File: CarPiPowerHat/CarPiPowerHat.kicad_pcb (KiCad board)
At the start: 4 copper layers, 96 x 85 mm, 118 parts, among them J1 HDMI_A_1.4, J2 1-84953-5, J3 40HAT, J4 Conn_02x03_Counter_Clockwise, J5 USB_A, J6 1-84953-5, J7 HDMI_A_1.4, J8 AudioJack2_Ground, Q1 DMG2305, Q1 DMMT5401, Q2 DMG2305UX, Q3 DMP3013SFV-7, U1 AP64501SP-13, U1 UDA1334ATS, U2 AP2112-3.3K, U2 CAT24C32, U3 LM3480-5.0, U4 ATtiny45V-10X, U5 PCF85063AT/AAZ, U6 RT9742SNGV, U8 UDA1334ATS, X2 19269, Y1 X32K768S301

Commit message: doing some traces
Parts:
- removed the C1 at (51.8, 100.4)
- removed the C11 at (29.0, 86.7)
- removed the C13 at (29.9, 92.9)
- removed the C14 at (51.3, 89.6)
- removed the C2 at (51.3, 91.4)
- removed the C3 at (55.7, 87.1)
- removed the C4 at (45.9, 99.5)
- removed the C5 at (50.3, 100.4)
- removed the C6 at (46.6, 90.5)
- removed the C7 at (39.7, 88.7)
- removed the C8 at (42.2, 99.5)
- removed the FB2 at (34.3, 88.2)
- removed the Q1 at (55.7, 90.7)
- removed the R1 at (56.9, 93.4)
- removed the R2 at (55.7, 88.3)
- removed the R3 at (42.2, 87.8)
- removed the R4 at (42.1, 89.6)
- removed the R5 at (48.7, 104.1)
- removed the R6 at (45.5, 104.1)
- removed the U1 at (52.2, 95.3)
- removed the U2 at (29.7, 89.7)
- removed X2: 19269, Adafruit I2S Audio UDA1334 Bonnet:4UCONN_19269
- added C27: 0.1uF, Capacitor_SMD:C_0603_1608Metric, F.Cu at (125.1, 74.5)
- added C28: 10uF, Capacitor_SMD:C_0805_2012Metric_Pad1.18x1.45mm_HandSolder, F.Cu at (121.6, 70.2)
- added C29: 10uF, Capacitor_SMD:C_0805_2012Metric, F.Cu at (119.0, 93.3)
- added C30: 0.1uF, Capacitor_SMD:C_0603_1608Metric, F.Cu at (121.0, 93.3)
- added C31: 10uF, Capacitor_SMD:C_0805_2012Metric_Pad1.18x1.45mm_HandSolder, F.Cu at (114.0, 70.2)
- added C32: 0.1uF, Capacitor_SMD:C_0603_1608Metric, F.Cu at (119.5, 83.8)
- added C33: 47uF, Capacitor_SMD:CP_Elec_6.3x7.7, F.Cu at (113.7, 79.6)
- added C34: 47uF, Capacitor_SMD:CP_Elec_6.3x7.7, F.Cu at (112.7, 91.6)
- added C35: 10uF, Capacitor_SMD:C_0805_2012Metric, F.Cu at (119.5, 81.8)
- added C36: 0.01uF, Capacitor_SMD:C_0603_1608Metric, F.Cu at (130.9, 100.3)
- added C37: 0.01uF, Capacitor_SMD:C_0603_1608Metric, F.Cu at (122.5, 102.3)
- added D5: D_TVS, Diode_SMD:D_0603_1608Metric_Pad1.05x0.95mm_HandSolder, F.Cu at (162.9, 94.3)
- added FB4: Ferrite, Resistor_SMD:R_0805_2012Metric, F.Cu at (116.2, 73.3)
- added J9: Conn_01x04, Connector_PinHeader_1.00mm:PinHeader_1x04_P1.00mm_Vertical, F.Cu at (81.0, 99.5)
- added Q4: DMG2305, Package_TO_SOT_SMD:SOT-23W_Handsoldering, F.Cu at (125.1, 80.3)
- added R22: 10K, Resistor_SMD:R_0603_1608Metric, F.Cu at (125.1, 76.3)
- added R23: 10K, Resistor_SMD:R_0603_1608Metric_Pad0.98x0.95mm_HandSolder, F.Cu at (126.2, 85.3)
- added R24: 220k, Resistor_SMD:R_0805_2012Metric, F.Cu at (118.5, 78.3)
- added R25: 220k, Resistor_SMD:R_0805_2012Metric, F.Cu at (117.9, 96.8)
- added R26: 100, Resistor_SMD:R_0603_1608Metric, F.Cu at (131.0, 98.6)
- added R27: 100, Resistor_SMD:R_0603_1608Metric, F.Cu at (122.5, 100.6)
- added R28: 10K 1%, Resistor_SMD:R_0603_1608Metric, F.Cu at (153.4, 58.3)
- added TP6: TestPoint, TestPoint:TestPoint_Pad_2.0x2.0mm, B.Cu at (102.7, 112.7)
- added TP7: TestPoint, TestPoint:TestPoint_Pad_2.0x2.0mm, B.Cu at (98.3, 112.7)
- added U7: AP2112-3.3K, Package_TO_SOT_SMD:SOT-23-5_HandSoldering, F.Cu at (117.8, 70.1)
- C13: footprint Capacitor_SMD:C_0402_1005Metric -> Capacitor_SMD:C_0603_1608Metric
- FB1: footprint Adafruit I2S Audio UDA1334 Bonnet:0805 -> Resistor_SMD:R_0805_2012Metric
- R11, R13, R14, R15, R16, R17, R19: footprint Resistor_SMD:R_0402_1005Metric -> Resistor_SMD:R_0603_1608Metric
- R18: value 320 1% -> 200 1%
- R3, R6, R8: footprint project_footprints:R_0603_1608Metric_Pad0.84x1.00mm_HandSolder -> Resistor_SMD:R_0603_1608Metric
- moved U6 131.6 mm to (145.6, 104.3), turned to -90 degrees
- moved C25 129.4 mm to (147.2, 102.0)
- moved C26 125.6 mm to (143.3, 102.6), turned to 90 degrees
- moved U8 103.7 mm to (121.2, 87.8), turned to 180 degrees
- moved D8 98.4 mm to (142.0, 82.6)
- moved D9 98.4 mm to (138.7, 82.6)
- moved C22 98.4 mm to (139.1, 91.8)
- moved D10 98.4 mm to (142.0, 88.2)
- moved FB2 98.4 mm to (138.8, 87.6)
- moved R20 98.4 mm to (142.7, 92.4)
- moved FB1 87.5 mm to (119.2, 74.4)
- moved U3 86.3 mm to (158.0, 69.8)
- moved C21 80.8 mm to (160.5, 70.6)
- moved R13 79.8 mm to (154.0, 67.2)
- moved C23 77.6 mm to (148.7, 90.9)
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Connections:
- net Net-(C21-Pad1) renamed /Power Control/VO
- net Net-(D6-Pad3) renamed /Power Control/VCC
- C20 pad 1: Net-(C20-Pad1) -> CAR_IGN
- C25 pad 1: /P5V_HAT -> /PSU/P5V
- F2 pad 2: Net-(C20-Pad1) -> CAR_IGN
- FB1 pad 1: (no net) -> AGND
- FB1 pad 2: (no net) -> GND
- J8 pad R: (no net) -> /i2s_dac/OUTR
- J8 pad S: /i2s_dac/OUTR -> AGND
- U3 pad 2: Net-(C20-Pad1) -> CAR_IGN
- U4 pad 2: Net-(R14-Pad1) -> /PSU/PSU_EN
- U4 pad 5: /PSU/PSU_EN -> Net-(R14-Pad1)
- U5 pad 3: /RTC Clock/nRTC_INT -> unconnected-(U5-Pad3)
- U6 pad 1: /P5V_HAT -> /PSU/P5V
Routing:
- net (no net): track 206.0 -> 0.00 mm, vias 8 -> 0
- net PWR_SENSE_OUT: track 0.00 -> 158.1 mm, vias 0 -> 3
- net Net-(R18-Pad1): track 0.00 -> 154.5 mm, vias 0 -> 2
- net /PSU/P5V: track 8.84 -> 134.3 mm, vias 0 -> 8
- net /SCL: track 0.00 -> 119.7 mm
- net /SDA: track 0.00 -> 117.8 mm, vias 0 -> 2
- net /+3.3v: track 8.18 -> 83.4 mm, vias 0 -> 2
- net /P5V_HAT: track 7.17 -> 80.5 mm
- net GND: track 60.8 -> 128.1 mm, vias 25 -> 146
- net /PSU/P12V: track 0.00 -> 54.6 mm, vias 0 -> 1
- net Net-(BT1-Pad1): track 0.00 -> 45.4 mm
- net Net-(C33-Pad2): track 0.00 -> 44.7 mm
- net CAR_IGN: track 0.00 -> 43.6 mm
- net /BITCLK: track 0.00 -> 42.9 mm, vias 0 -> 2
- net /HDMI Connector Camera/D0-: track 0.00 -> 34.3 mm, vias 0 -> 1
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- added copper zone on F.Cu, net /PSU/P12V
- added copper zone on F.Cu, net AGND
- added copper zone on In2.Cu, net AGND
- added copper zone on B.Cu, net GND
- added copper zone on F.Cu, net GND
- added copper zone on In1.Cu, net GND
- added copper zone on F.Cu, net Net-(L1-Pad1)
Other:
- board text added: "D C B A"
- board text removed: "If you want to use an SMT 40-pin header, please move the top edge up by 0.5mm and locate the header in the same location as the current TH part."

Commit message: Everything routed, DRC ok
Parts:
- removed U6: RT9742SNGV, Package_TO_SOT_SMD:SOT-23
- added D11: D_TVS, Diode_SMD:D_0603_1608Metric, F.Cu at (150.7, 88.9)
- added D7: D_TVS, Diode_SMD:D_0603_1608Metric, F.Cu at (150.8, 78.6)
- added IC1: AP2331TDSA-7, ap2331:SOT96P240X110-3N, F.Cu at (145.6, 104.1)
- added J10: Conn_01x02_Male, Connector_JST:JST_XH_S2B-XH-A_1x02_P2.50mm_Horizontal, B.Cu at (144.8, 61.8)
- moved C22 18.3 mm to (149.1, 76.5), turned to 90 degrees
- moved R20 13.8 mm to (146.8, 79.2)
- moved FB2 12.1 mm to (148.8, 80.9), turned to 90 degrees
- moved D9 10.8 mm to (147.0, 75.7), turned to 90 degrees
- moved D12 10.3 mm to (143.1, 87.3), turned to 0 degrees
- moved D14 8.26 mm to (144.3, 91.0), turned to 90 degrees
- moved D10 8.17 mm to (144.4, 80.4), turned to 90 degrees
- moved R21 6.15 mm to (146.4, 89.7)
- moved D8 5.94 mm to (143.2, 76.8), turned to 0 degrees
- moved D13 4.80 mm to (146.8, 86.2), turned to 90 degrees
- moved FB3 4.43 mm to (148.7, 91.1), turned to 90 degrees
- moved C23 3.84 mm to (148.9, 87.1), turned to 90 degrees
- moved C20 1.79 mm to (156.6, 72.2), turned to 180 degrees
- moved C25 1.15 mm to (146.1, 101.6)
- moved C11 0.43 mm to (169.2, 56.9)
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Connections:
- net /BCM16 renamed /MUTE
- net /ID_SC_EEPROM renamed /Raspberry Pi/ID_SC_EEPROM
- net /ID_SD_EEPROM renamed /Raspberry Pi/ID_SD_EEPROM
- net /P5V_HAT renamed /Raspberry Pi/P5V_HAT
- net /SCL renamed /HDMI Connector Display/B
- net /SDA renamed /RTC Clock/SDA
- net /i2s_dac/MUTE renamed Net-(Q4-Pad3)
- net /i2s_dac/VDD renamed /i2s_dac/VDDA
- net LIGHT_SENSE renamed /Light Input/OUT
- net PWR_SENSE_IN renamed /Power Control/PWR_SENSE_IN
- net REVERSE_SENSE renamed /Raspberry Pi/BCM25
- C20 pad 1: CAR_IGN -> Net-(C20-Pad1)
- D5 pad 2: CAR_IGN -> Net-(C20-Pad1)
- F2 pad 2: CAR_IGN -> Net-(C20-Pad1)
- U3 pad 2: CAR_IGN -> Net-(C20-Pad1)
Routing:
- net /+3.3v: track 83.4 -> 123.6 mm, vias 2 -> 4
- net PWR_SENSE_OUT: track 158.1 -> 123.3 mm
- net GND: track 128.1 -> 160.1 mm, vias 146 -> 265
- net CAR_IGN: track 43.6 -> 12.5 mm
- net Net-(R18-Pad1): track 154.5 -> 123.5 mm
- net Net-(C20-Pad1): track 0.00 -> 29.6 mm
- net CAR_REVERSE: track 0.00 -> 24.2 mm
- net /Light Input/OUT: track 16.2 -> 36.8 mm
- net /RTC Clock/SDA: track 117.8 -> 134.2 mm, vias 2 -> 3
- net CAR_LIGHT: track 0.00 -> 12.7 mm
- net /HDMI Connector Display/B: track 119.7 -> 131.4 mm, vias 0 -> 1
- net Net-(C22-Pad1): track 0.00 -> 10.4 mm
- net Net-(C23-Pad1): track 0.00 -> 10.1 mm
- net /Raspberry Pi/BCM25: track 16.6 -> 26.1 mm
- net /PSU/P5V: track 134.3 -> 138.0 mm
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- added copper zone on F.Cu, net /PSU/USB_5v
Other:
- board text added: "2.5A"
- board text added: "500mA"
- board text added: "WP"

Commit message: Cleanup
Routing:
- net /HDMI Connector Display/B: track 131.4 -> 129.8 mm

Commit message: Finalizing
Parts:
- removed R2: DNP, project_footprints:R_0603_1608Metric_Pad0.84x1.00mm_HandSolder
- added JP1: SolderJumper_2_Open, Jumper:SolderJumper-2_P1.3mm_Open_RoundedPad1.0x1.5mm, F.Cu at (136.5, 66.5)
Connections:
- net /HDMI Connector Display/B renamed /RTC Clock/SCL
- net /Raspberry Pi/P5V_HAT renamed /i2s_dac/+5v
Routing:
- net /RTC Clock/SCL: track 129.8 -> 131.9 mm
- net Net-(R3-Pad2): track 11.4 -> 13.4 mm
- net GND: track 160.0 -> 159.1 mm, vias 265 -> 275
- net /Raspberry Pi/BCM25: track 26.1 -> 26.6 mm
- net /Light Input/OUT: track 36.8 -> 37.4 mm
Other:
- board text added: "12V"
- board text added: "Camera"
- board text added: "Display"
- board text added: "GND"
- board text added: "IGN"
- board text added: "Light"
- board text added: "Line Out"
- board text added: "OpenAuto Raspberry Pi HAT"
- board text added: "Power"
- board text added: "Rev"

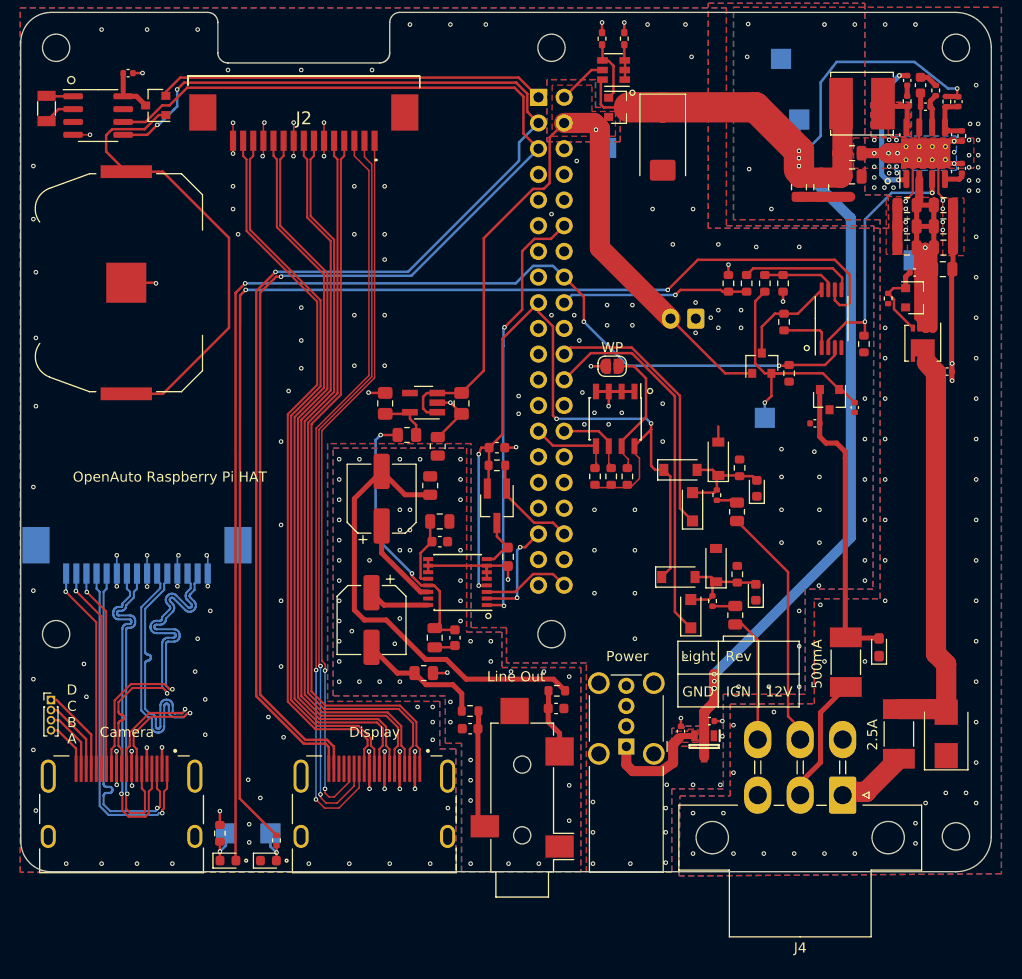
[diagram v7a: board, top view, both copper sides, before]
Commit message: Repositioning of connectors
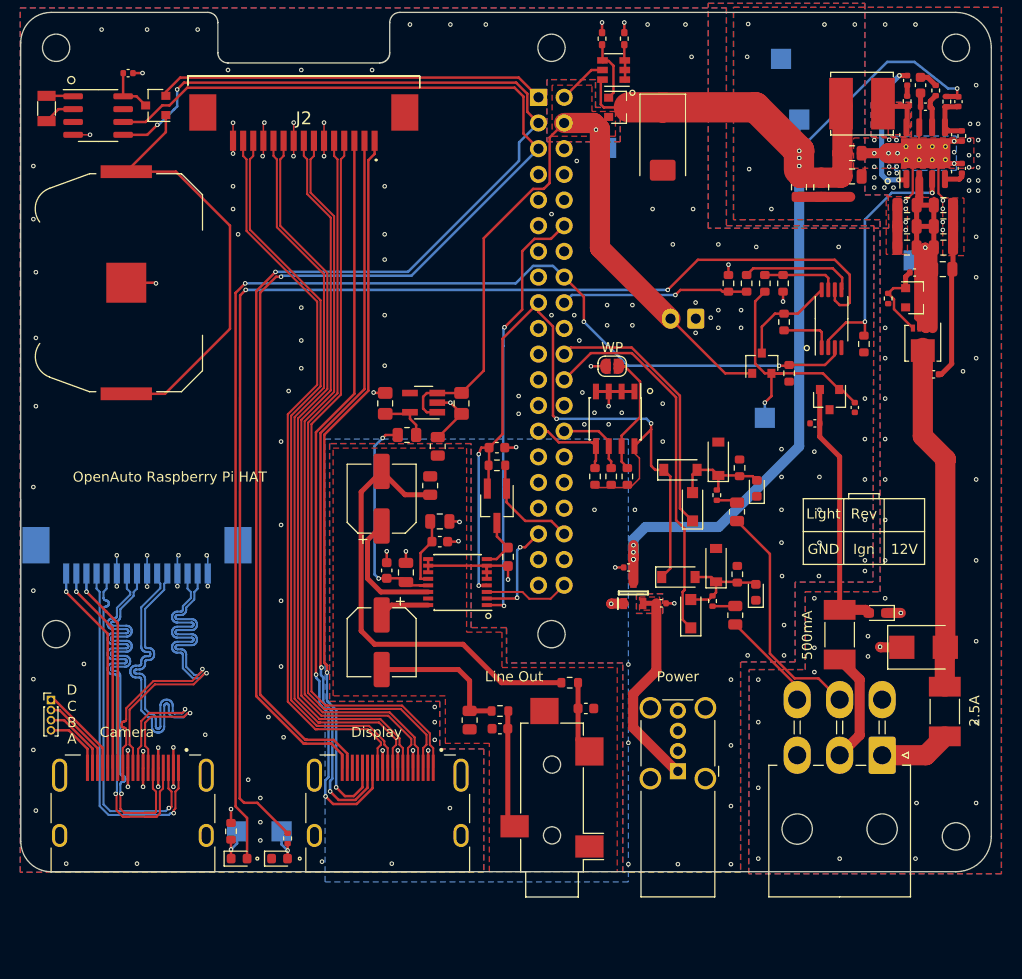
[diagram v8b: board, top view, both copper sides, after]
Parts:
- J4: footprint Connector_Molex:Molex_Mini-Fit_Jr_5569-06A1_2x03_P4.20mm_Horizontal -> Connector_Molex:Molex_Mini-Fit_Jr_5569-06A2_2x03_P4.20mm_Horizontal
- moved C25 17.2 mm to (138.1, 86.4), turned to 180 degrees
- moved IC1 16.7 mm to (138.6, 88.9), turned to 90 degrees
- moved C26 12.8 mm to (141.4, 89.9), turned to 0 degrees
- moved C30 9.48 mm to (114.2, 86.7), turned to 90 degrees
- moved D3 8.86 mm to (167.3, 94.3), turned to 0 degrees
- moved C29 7.05 mm to (116.1, 86.9), turned to 90 degrees
- moved R25 6.50 mm to (122.4, 101.5), turned to 90 degrees
- moved J5 5.66 mm to (143.0, 106.6)
- moved J4 5.55 mm to (163.2, 105.0)
- moved F1 5.05 mm to (169.4, 100.6)
- moved D5 3.40 mm to (162.8, 90.9), turned to 180 degrees
- moved C36 2.95 mm to (133.9, 100.3)
- moved J8 2.95 mm to (130.6, 110.4)
- moved C37 2.95 mm to (125.4, 102.3)
- moved R27 2.95 mm to (125.4, 100.6)
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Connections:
- net Net-(C32-Pad1) renamed /i2s_dac/VREF
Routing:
- net /PSU/P5V: track 138.0 -> 121.4 mm
- net /HDMI Connector Camera/D1+: track 33.0 -> 45.8 mm
- net /HDMI Connector Camera/D1-: track 34.2 -> 46.5 mm
- net /PSU/USB_5v: track 11.0 -> 20.9 mm
- net Net-(C4-Pad1): track 40.2 -> 35.3 mm
- net Net-(C29-Pad1): track 26.6 -> 22.0 mm
- net Net-(C20-Pad1): track 29.6 -> 25.6 mm
- net Net-(C33-Pad1): track 8.87 -> 12.3 mm
- net /HDMI Connector Camera/CK+: track 34.3 -> 37.3 mm
- net Net-(BT1-Pad1): track 45.8 -> 42.8 mm
- net CAR_LIGHT: track 12.7 -> 9.97 mm
- net /HDMI Connector Camera/D2+: track 34.3 -> 36.6 mm
- net /HDMI Connector Camera/D0+: track 34.4 -> 36.7 mm
- net /HDMI Connector Camera/CK-: track 34.5 -> 36.6 mm
- net Net-(C34-Pad2): track 12.5 -> 14.3 mm
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- removed copper zone on B.Cu, net AGND
- removed copper zone on In2.Cu, net AGND
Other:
- board text added: "Ign"
- board text removed: "IGN"
